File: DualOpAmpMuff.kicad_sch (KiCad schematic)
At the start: 97 parts, among them J101 IO, Q101 2N7002, Q102 2N7002, SW101 SW_SPDT, SW102 SW_SPDT, U101 LM324, U102 RC4558

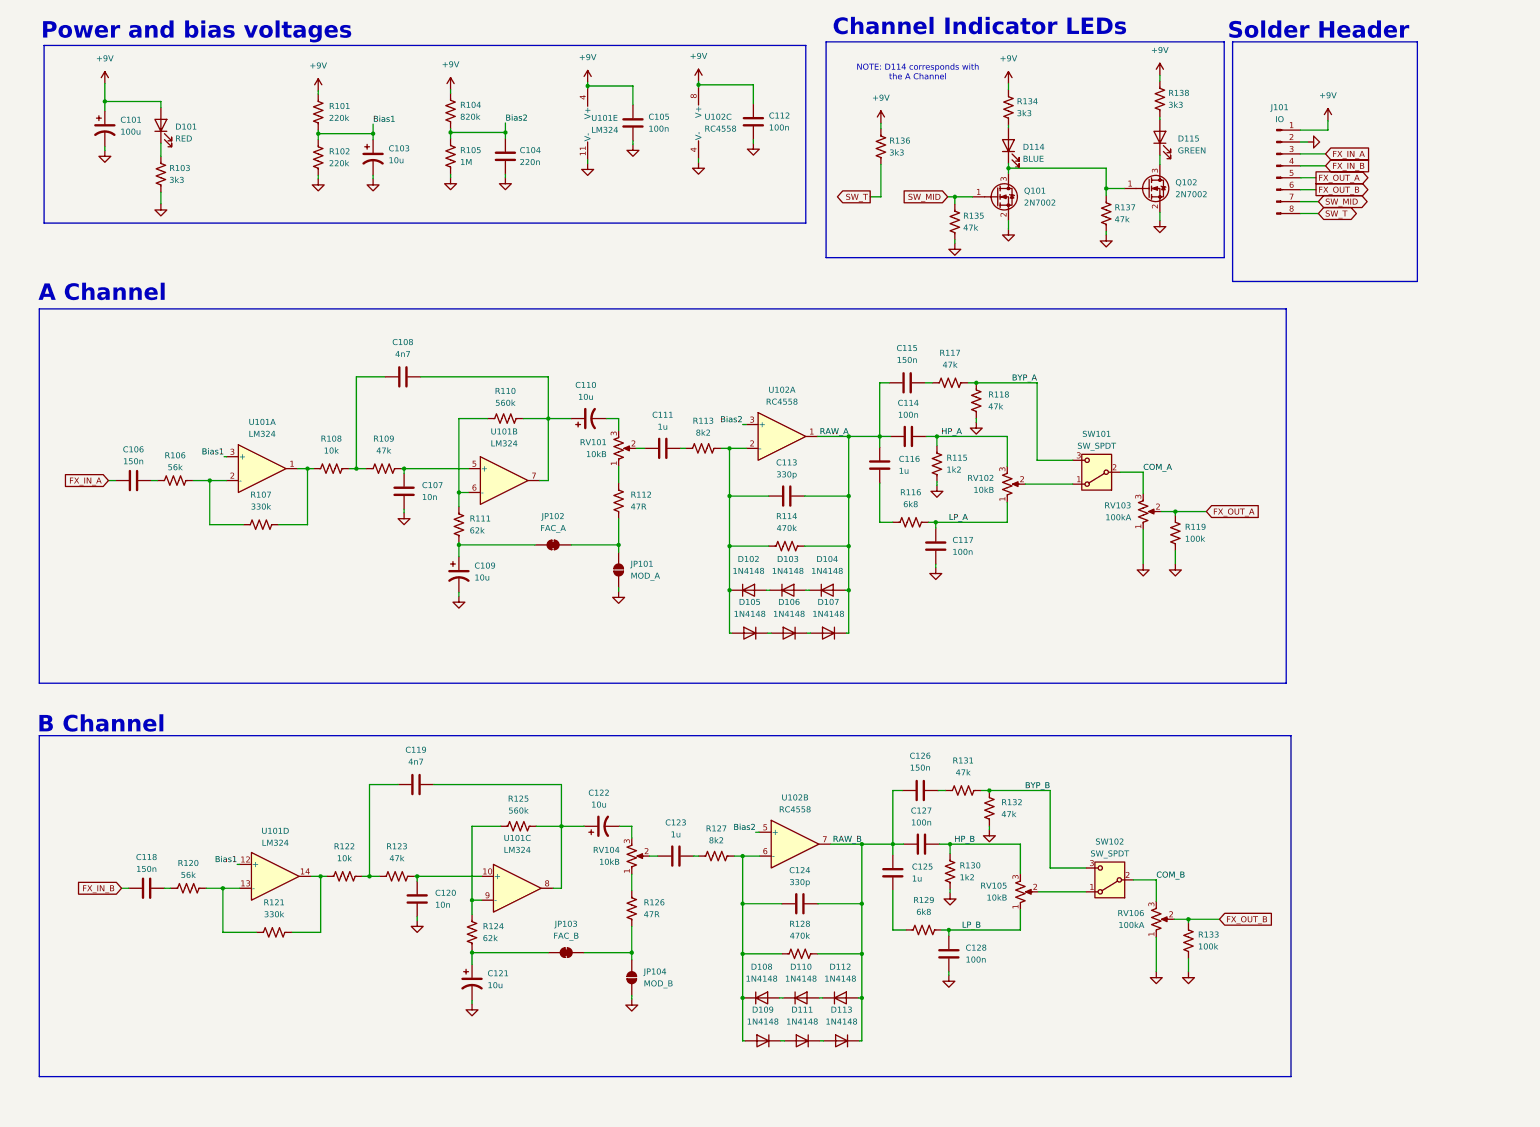
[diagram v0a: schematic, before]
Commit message: switched to 2 layer
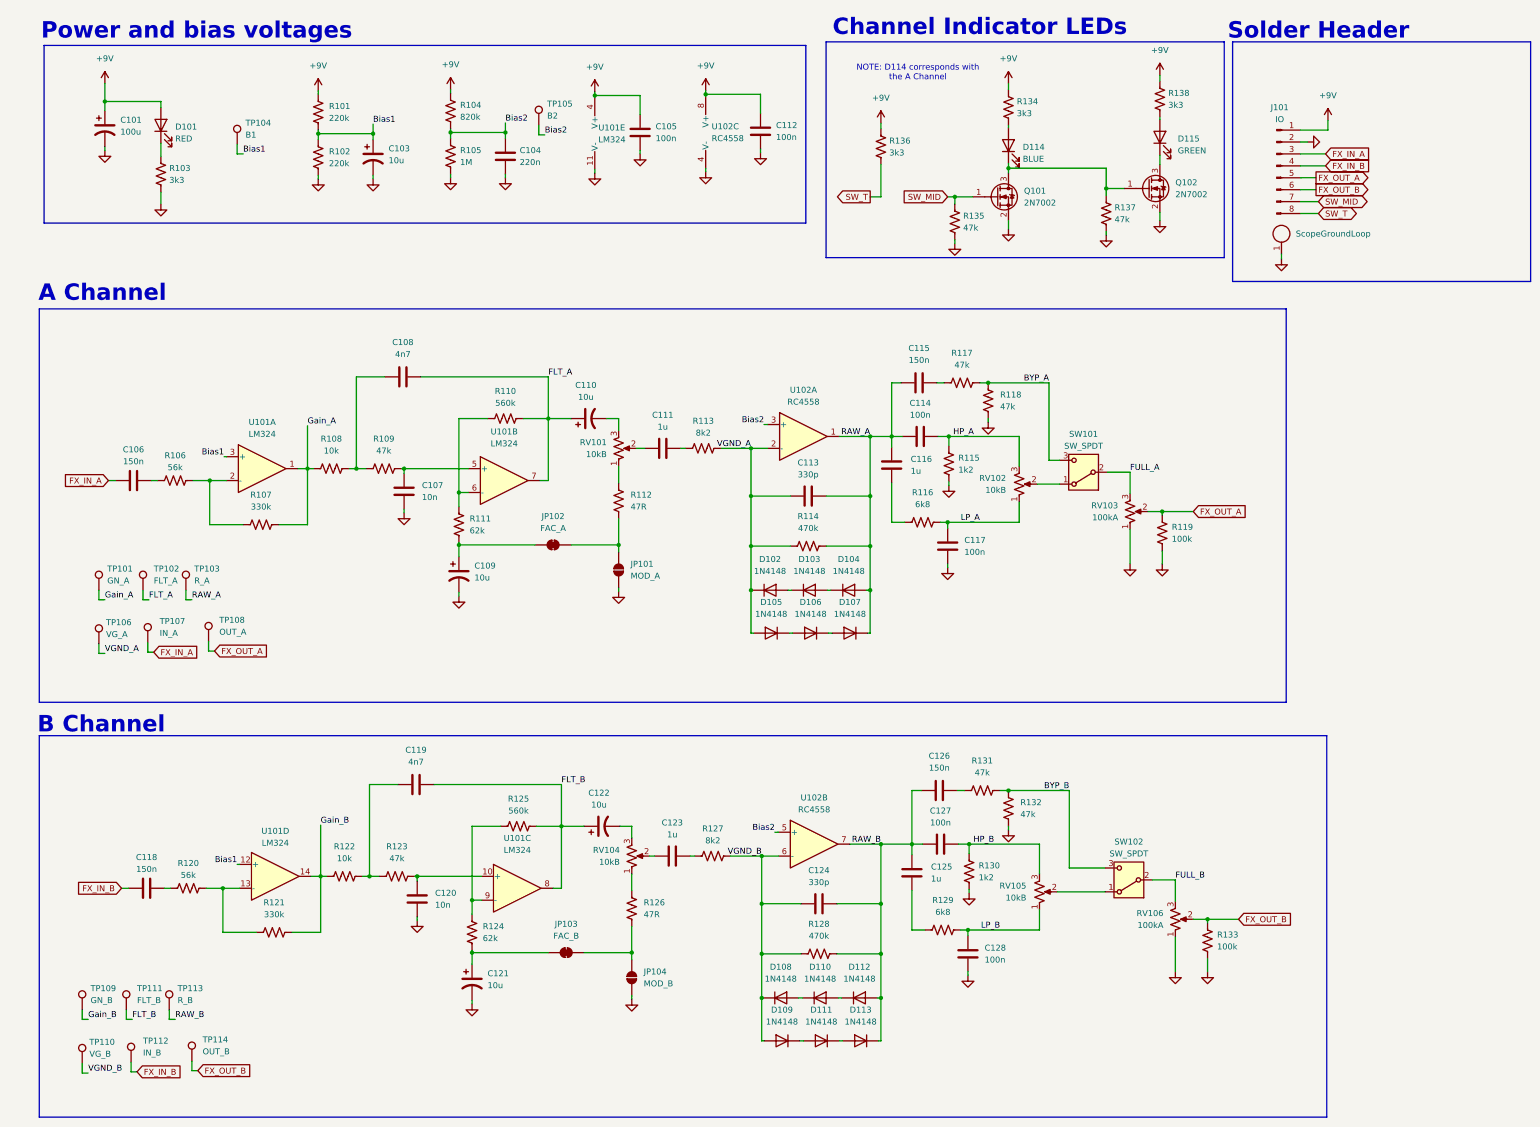
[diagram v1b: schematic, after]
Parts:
- added J102: ScopeGroundLoop, Connector:THT_GND_WIRE, symbol Connector:ScopeGroundLoop
- added TP101: GN_A, TestPoint:TestPoint_THTPad_D2.0mm_Drill1.0mm_VAL, symbol Connector:TestPoint
- added TP102: FLT_A, TestPoint:TestPoint_THTPad_D2.0mm_Drill1.0mm_VAL, symbol Connector:TestPoint
- added TP103: R_A, TestPoint:TestPoint_THTPad_D2.0mm_Drill1.0mm_VAL, symbol Connector:TestPoint
- added TP104: B1, TestPoint:TestPoint_THTPad_D2.0mm_Drill1.0mm_VAL, symbol Connector:TestPoint
- added TP105: B2, TestPoint:TestPoint_THTPad_D2.0mm_Drill1.0mm_VAL, symbol Connector:TestPoint
- added TP106: VG_A, TestPoint:TestPoint_THTPad_D2.0mm_Drill1.0mm_VAL, symbol Connector:TestPoint
- added TP107: IN_A, TestPoint:TestPoint_THTPad_D2.0mm_Drill1.0mm_VAL, symbol Connector:TestPoint
- added TP108: OUT_A, TestPoint:TestPoint_THTPad_D2.0mm_Drill1.0mm_VAL, symbol Connector:TestPoint
- added TP109: GN_B, TestPoint:TestPoint_THTPad_D2.0mm_Drill1.0mm_VAL, symbol Connector:TestPoint
- added TP110: VG_B, TestPoint:TestPoint_THTPad_D2.0mm_Drill1.0mm_VAL, symbol Connector:TestPoint
- added TP111: FLT_B, TestPoint:TestPoint_THTPad_D2.0mm_Drill1.0mm_VAL, symbol Connector:TestPoint
- added TP112: IN_B, TestPoint:TestPoint_THTPad_D2.0mm_Drill1.0mm_VAL, symbol Connector:TestPoint
- added TP113: R_B, TestPoint:TestPoint_THTPad_D2.0mm_Drill1.0mm_VAL, symbol Connector:TestPoint
- added TP114: OUT_B, TestPoint:TestPoint_THTPad_D2.0mm_Drill1.0mm_VAL, symbol Connector:TestPoint
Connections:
- net Bias1: now also TP104.1
- net Bias2: now also TP105.1
- net FX_IN_A: now also TP107.1
- net FX_IN_B: now also TP112.1
- net FX_OUT_A: now also TP108.1
- net FX_OUT_B: now also TP114.1
- net GND: now also J102.1
- net RAW_A: now also TP103.1
- net RAW_B: now also TP113.1
- net Gain_B: now reaches R121.2, R122.1, U101.14
- net Gain_B: now also TP109.1
- net VGND_A: now reaches C113.1, D102.1 (K), D105.2 (A), R113.2, R114.1, U102.2 (-)
- net VGND_A: now also TP106.1
- net VGND_B: now reaches C124.1, D108.1 (K), D109.2 (A), R127.2, R128.1, U102.6 (-)
- net VGND_B: now also TP110.1
- net FLT_B: now reaches C119.2, C122.1, R125.2, U101.8
- net FLT_B: now also TP111.1
- net FLT_A: now reaches C108.2, C110.1, R110.2, U101.7
- net FLT_A: now also TP102.1
- net Gain_A: now reaches R107.2, R108.1, U101.1
- net Gain_A: now also TP101.1
- net COM_A renamed FULL_A
- net COM_B renamed FULL_B
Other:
- moved on the sheet: C105, C112, C113, C114, C115, C116, C117, C123, C124, C125, C126, C127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

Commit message: smaller outline laid out
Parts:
- removed C103: 10u, Capacitor_SMD:C_0805_2012Metric, symbol Device:C_Polarized_US
- removed C109, C110, C121, C122: 10u, Capacitor_THT:CP_Radial_D5.0mm_P2.50mm, symbol Device:C_Polarized_US
- removed TP101: GN_A, TestPoint:TestPoint_THTPad_D2.0mm_Drill1.0mm_VAL, symbol Connector:TestPoint
- removed TP106: VG_A, TestPoint:TestPoint_THTPad_D2.0mm_Drill1.0mm_VAL, symbol Connector:TestPoint
- removed TP109: GN_B, TestPoint:TestPoint_THTPad_D2.0mm_Drill1.0mm_VAL, symbol Connector:TestPoint
- removed TP110: VG_B, TestPoint:TestPoint_THTPad_D2.0mm_Drill1.0mm_VAL, symbol Connector:TestPoint
- added C102, C103, C109, C110, C121: 10u, Capacitor_SMD:C_0805_2012Metric, symbol Device:C
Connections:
- net Bias1: now also C103.1
- net FLT_A: now also C109.2
- net FLT_B: now also C121.1
- net GND: now also C102.2, C103.2, C110.2
- net at RV101.3: now also C109.1
- net at JP102.1 (A), R111.2: now also C102.1
- net at RV104.3: now also C121.2
- net at JP103.1 (A), R124.2: now also C110.1
